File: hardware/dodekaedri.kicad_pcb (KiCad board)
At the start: 4 copper layers, 76.2 x 76.2 mm, 229 parts, among them CON401 BARREL_JACK, J801 HANDSFREE, P301 BNC, P801 TX_SW_WIRE, P802 USB_OTG, P803 UART, P804 PROG, P805 RNG_PINS, P806 CONN_01X08, P807 CONN_01X04, P808 CONN_02X04, P809 BOOT0JMPR, Q501 BCP56, Q502 IRL510, Q801 BSS84, SW801 SW_PUSH, SW802 SW, SW803 SW, SW804 SW, SW806 encoder, SW807 RESET, T301 TRANSFO, T302 TRANSFO, T501 TRANSFO2, T601 TRANSFO2, U201 MIC5365, U202 SI5351A, U401 NCP3170-D, U501 74LVC1G3157, U502 74LVC1G3157, U601 74LVC1G3157, U602 74LVC1G3157, U603 TL972IDR, U701 WM8731, U702 MCP6L02, U801 STM32F401, U802 WM8731

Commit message: Changed some component values
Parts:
- C804: value 1n -> 1nF
- D301, D302, D303, D818, D819, D820, D821, D822, D823: value BAT54 -> BAT54SL
- D304, D305, D306: value BAP65-02 -> BA891
- D805, D806, D807, D809, D810, D812: value 1N914 -> BAT54SL
- R201, R202, R703, R812, R814, R816: value 10k -> 1k
- R203, R204, R205, R206, R207, R503, R818, R819, R823, R824: value 50R -> 100R
- R301, R822: value 10k -> 7k87
- R302, R303: value 50R -> 47R
- R701, R702, R810, R811: value 10k -> 0.1pF
- R801, R805, R807: value 10k -> 100k
- R802, R804: value 100R -> 1k

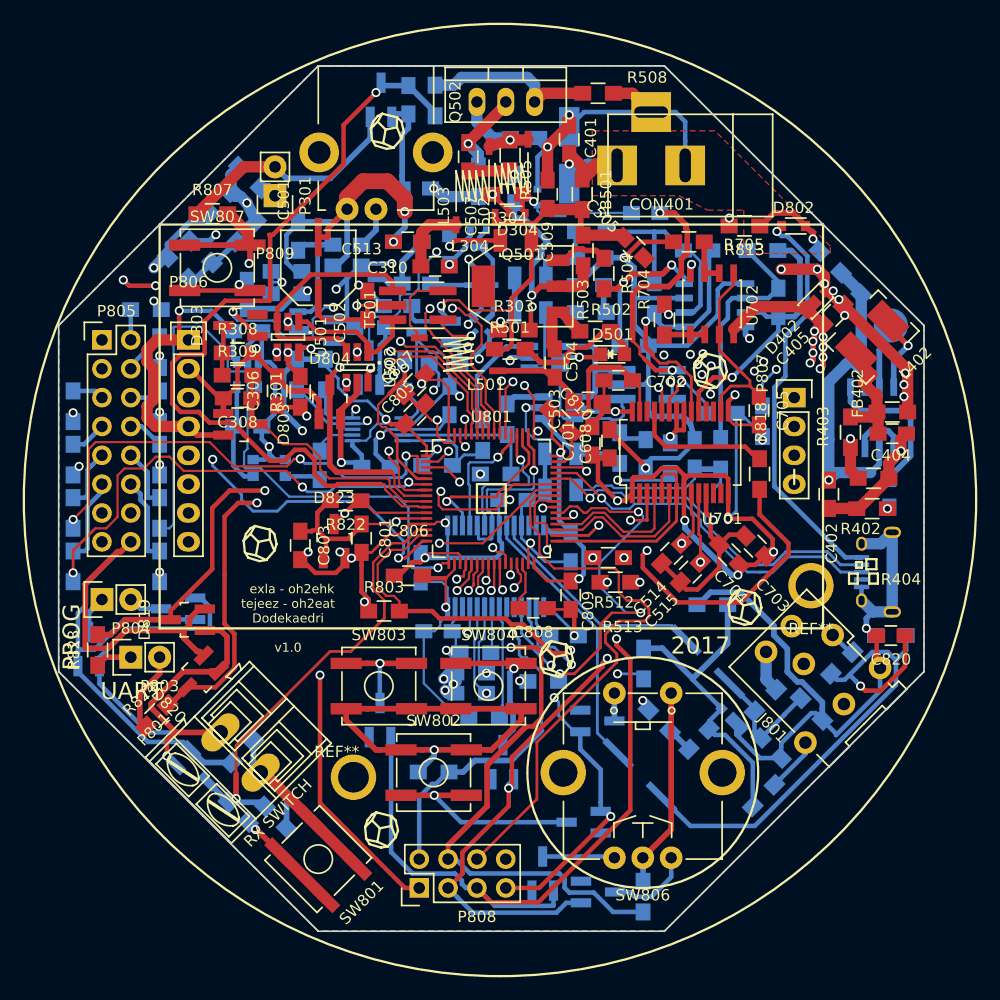
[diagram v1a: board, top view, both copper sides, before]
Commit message: Changed TX driver supply voltage to 3.3V
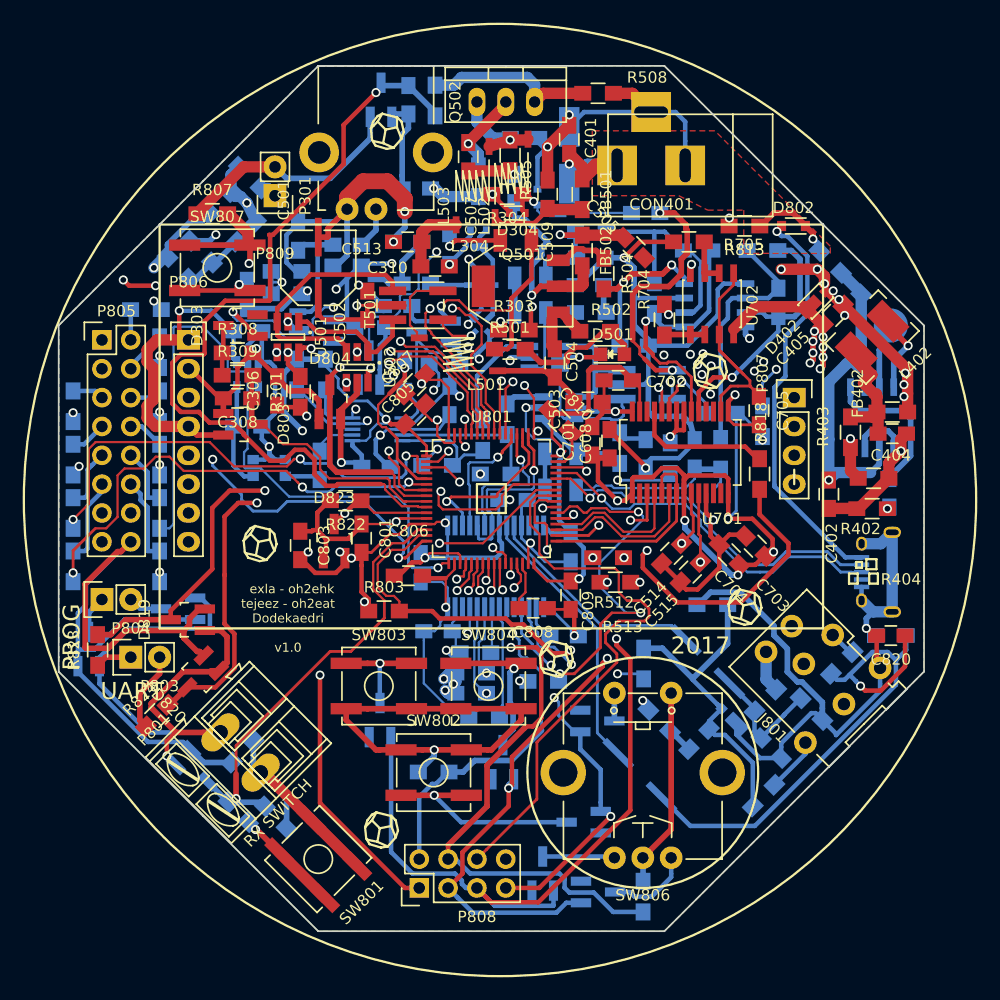
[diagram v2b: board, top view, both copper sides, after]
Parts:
- removed R503: 100R, Resistors_SMD:R_0805_HandSoldering
- removed REF** (x2): m2.5_mounting_hole_small, dodekaedri:m2.5_mounting_hole_small
- added FB502: FILTER, Resistors_SMD:R_0805_HandSoldering, F.Cu at (151.5, 63.2)
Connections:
- C505 pad 1: Net-(C505-Pad1) -> +Vlogic
- C509 pad 1: Net-(C505-Pad1) -> Net-(C509-Pad1)
- FB501 pad 2: Net-(C505-Pad1) -> Net-(C509-Pad1)
- L502 pad 1: Net-(C505-Pad1) -> Net-(C509-Pad1)
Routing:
- net Net-(C505-Pad1): track 14.7 -> 0.00 mm
- net Net-(C509-Pad1): track 0.00 -> 8.88 mm
- net +Vlogic: track 409.8 -> 415.4 mm, vias 39 -> 40
